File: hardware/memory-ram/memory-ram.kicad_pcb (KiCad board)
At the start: 2 copper layers, 77 x 39 mm, 27 parts, among them J1 Conn_Mem_Ext, J2 Conn_Power, U1 IS61WV5128EDBLL-10TLI, U2 74LVC1G86, U3 MIC5504-3.3YM5, U4 74LVC1G32, U5 74LVC1G332, U6 74LVC1G86, U7 74LVC1G04

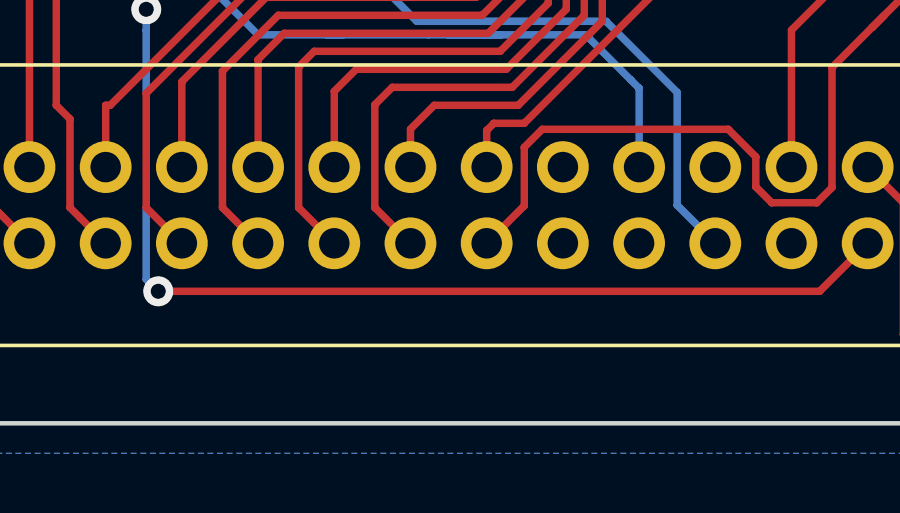
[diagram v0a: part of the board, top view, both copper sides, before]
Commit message: Added placeholders for JLCPCB serial numbers
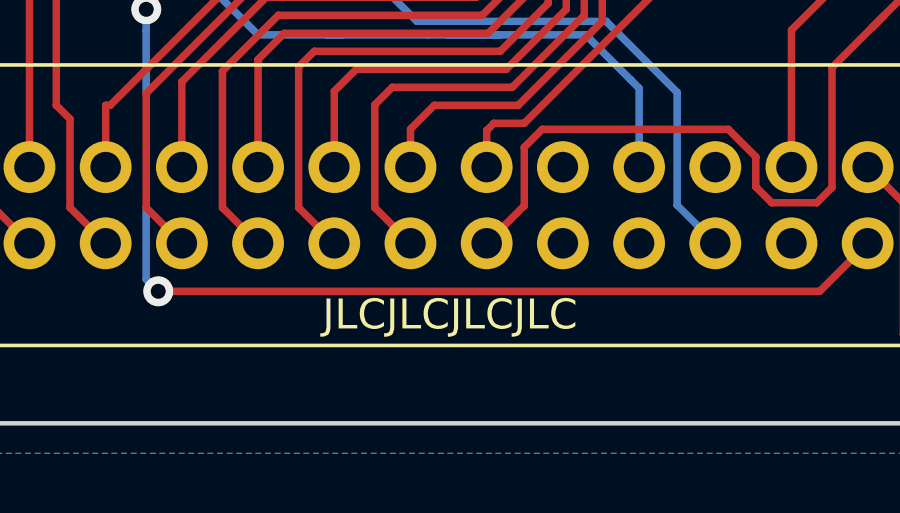
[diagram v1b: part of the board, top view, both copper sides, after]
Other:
- board text added: "JLCJLCJLCJLC"
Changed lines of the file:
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@@
   (general
     (thickness 1.6)
-    (drawings 18)
+    (drawings 19)
     (tracks 513)
     (zones 0)
@@
     )
   )
+  (gr_text JLCJLCJLCJLC (at 101.525 129.375) (layer F.SilkS)
+    (effects (font (size 1 1) (thickness 0.15)))
+  )
   (gr_text GND (at 136.25 120) (layer B.SilkS)
